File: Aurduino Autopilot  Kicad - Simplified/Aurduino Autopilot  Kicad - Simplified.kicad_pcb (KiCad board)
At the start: 2 copper layers, 79 x 74 mm, 24 parts, among them J1 12V_in, J2 to_clock, J3 to_LCD, J5 to_RTC, SW1 SW_Push, U1 LM350_TO3

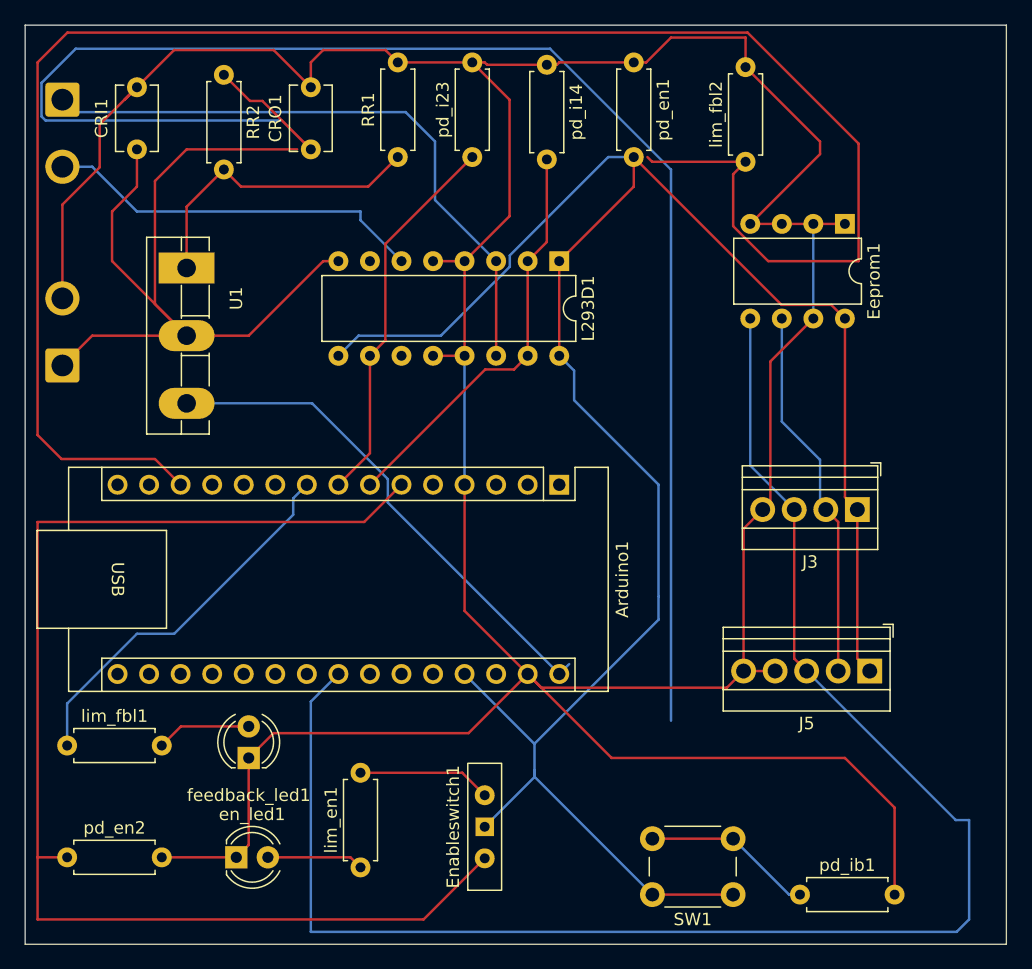
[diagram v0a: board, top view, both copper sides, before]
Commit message: added Simplified kicad design
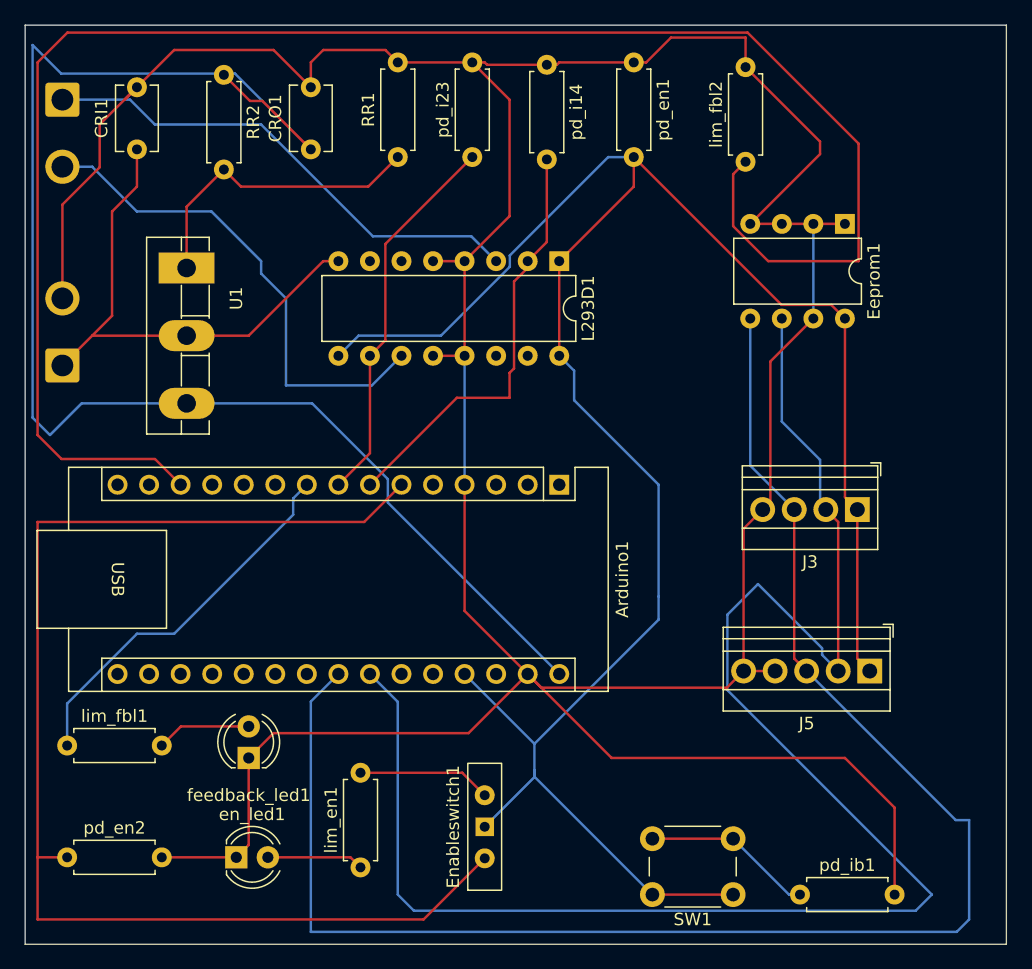
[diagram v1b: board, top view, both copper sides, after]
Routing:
- net Net-(Arduino1-A5): track 30.3 -> 135.5 mm
- net Net-(Arduino1-VIN): track 177.0 -> 119.5 mm
- net +12C: track 70.0 -> 42.2 mm
- net Net-(J2-Pin_2): track 30.9 -> 40.3 mm
- net Net-(J2-Pin_1): track 50.7 -> 41.7 mm
- net Net-(Arduino1-D10): track 148.4 -> 140.3 mm
- net Net-(Arduino1-D4): track 33.4 -> 34.6 mm
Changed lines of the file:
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@@
 	)
 	(segment
-		(start 42 75)
-		(end 36 69)
+		(start 38 60)
+		(end 38 63)
+		(width 0.2)
+		(layer "F.Cu")
+		(net 2)
+	)
+	(segment
+		(start 36 65)
+		(end 36 73.4)
 		(width 0.2)
 		(layer "F.Cu")
@@
 	)
 	(segment
-		(start 38 63)
-		(end 38 60)
-		(width 0.2)
-		(layer "F.Cu")
-		(net 2)
-	)
-	(segment
-		(start 36 65)
-		(end 38 63)
-		(width 0.2)
-		(layer "F.Cu")
-		(net 2)
-	)
-	(segment
-		(start 39.45 62.55)
-		(end 42 60)
-		(width 0.2)
-		(layer "F.Cu")
-		(net 2)
-	)
-	(segment
 		(start 42 75)
 		(end 47 75)
@@
 	)
 	(segment
-		(start 36 69)
-		(end 36 65)
-		(width 0.2)
-		(layer "F.Cu")
-		(net 2)
-	)
-	(segment
-		(start 42 60)
-		(end 50.9 60)
-		(width 0.2)
-		(layer "F.Cu")
-		(net 2)
-	)
-	(segment
-		(start 42 75)
-		(end 39.45 72.45)
+		(start 36 73.4)
+		(end 34.4 75)
 		(width 0.2)
 		(layer "F.Cu")
@@
 	)
 	(segment
-		(start 39.45 72.45)
-		(end 39.45 62.55)
+		(start 38 63)
+		(end 36 65)
 		(width 0.2)
 		(layer "F.Cu")
@@
 	)
 	(segment
-		(start 66.04 77.72)
-		(end 56.76 87)
+		(start 69.46 69.54)
+		(end 68.36 70.64)
 		(width 0.2)
 		(layer "F.Cu")
@@
 	)
 	(segment
-		(start 68.36 77.72)
-		(end 66.04 77.72)
+		(start 56.76 87)
+		(end 63.76 80)
 		(width 0.2)
 		(layer "F.Cu")
@@
 	)
 	(segment
+		(start 63.76 80)
+		(end 68 80)
+		(width 0.2)
+		(layer "F.Cu")
+		(net 3)
+	)
+	(segment
+		(start 68.36 70.64)
+		(end 68.36 77.64)
+		(width 0.2)
+		(layer "F.Cu")
+		(net 3)
+	)
+	(segment
 		(start 69.46 69)
-		(end 69.46 76.62)
-		(width 0.2)
-		(layer "F.Cu")
-		(net 3)
-	)
-	(segment
-		(start 69.46 76.62)
-		(end 68.36 77.72)
+		(end 69.46 69.54)
 		(width 0.2)
 		(layer "F.Cu")
@@
 	)
 	(segment
+		(start 68 80)
+		(end 68 78)
+		(width 0.2)
+		(layer "F.Cu")
+		(net 3)
+	)
+	(segment
+		(start 68.36 77.64)
+		(end 68 78)
+		(width 0.2)
+		(layer "F.Cu")
+		(net 3)
+	)
+	(segment
 		(start 52 53)
 		(end 53 52)
@@
 	)
 	(segment
-		(start 30.640256 57.675)
-		(end 30.325 57.359744)
+		(start 45.9 53.9)
+		(end 31.9 53.9)
 		(width 0.2)
 		(layer "B.Cu")
@@
 	)
 	(segment
+		(start 31 83)
+		(end 33.55 80.45)
+		(width 0.2)
+		(layer "B.Cu")
+		(net 9)
+	)
+	(segment
+		(start 29.6 51.6)
+		(end 29.6 81.6)
+		(width 0.2)
+		(layer "B.Cu")
+		(net 9)
+	)
+	(segment
 		(start 52 60)
-		(end 49.675 57.675)
+		(end 45.9 53.9)
 		(width 0.2)
 		(layer "B.Cu")
@@
 	)
 	(segment
-		(start 42 80.45)
-		(end 41.434365 80.45)
+		(start 33.55 80.45)
+		(end 42 80.45)
 		(width 0.2)
 		(layer "B.Cu")
@@
 	)
 	(segment
-		(start 49.675 57.675)
-		(end 30.640256 57.675)
-		(width 0.2)
-		(layer "B.Cu")
-		(net 9)
-	)
-	(segment
-		(start 81 61.634365)
-		(end 81 106)
-		(width 0.2)
-		(layer "B.Cu")
-		(net 9)
-	)
-	(segment
-		(start 33.065256 51.9)
-		(end 71.265635 51.9)
-		(width 0.2)
-		(layer "B.Cu")
-		(net 9)
-	)
-	(segment
-		(start 72 102.24)
-		(end 72.799999 101.440001)
-		(width 0.2)
-		(layer "B.Cu")
-		(net 9)
-	)
-	(segment
-		(start 30.325 54.640256)
-		(end 33.065256 51.9)
+		(start 31.9 53.9)
+		(end 29.6 51.6)
 		(width 0.2)
 		(layer "B.Cu")
@@
 	)
 	(segment
-		(start 30.325 57.359744)
-		(end 30.325 54.640256)
+		(start 29.6 81.6)
+		(end 31 83)
 		(width 0.2)
 		(layer "B.Cu")
@@
 	)
 	(segment
-		(start 71.265635 51.9)
-		(end 81 61.634365)
-		(width 0.2)
-		(layer "B.Cu")
-		(net 9)
-	)
-	(segment
-		(start 79.48 61)
-		(end 79.1 60.62)
-		(width 0.2)
-		(layer "F.Cu")
-		(net 12)
-	)
-	(segment
 		(start 96.1 59.534315)
 		(end 96.1 69)
@@
 	)
 	(segment
-		(start 87 61)
-		(end 79.48 61)
-		(width 0.2)
-		(layer "F.Cu")
-		(net 12)
-	)
-	(segment
 		(start 30 53)
 		(end 32.4 50.6)
@@
 	)
 	(segment
+		(start 48 69)
+		(end 48 70)
+		(width 0.2)
+		(layer "B.Cu")
+		(net 19)
+	)
+	(segment
 		(start 32 61.4)
 		(end 34.4 61.4)
@@
 	(segment
 		(start 38 65)
-		(end 56 65)
+		(end 44 65)
 		(width 0.2)
 		(layer "B.Cu")
@@
 	)
 	(segment
-		(start 56 65.7)
-		(end 59.3 69)
+		(start 50 79)
+		(end 56.92 79)
+		(width 0.2)
+		(layer "B.Cu")
+		(net 19)
+	)
+	(segment
+		(start 44 65)
+		(end 48 69)
+		(width 0.2)
+		(layer "B.Cu")
+		(net 19)
+	)
+	(segment
+		(start 48 70)
+		(end 50 72)
+		(width 0.2)
+		(layer "B.Cu")
+		(net 19)
+	)
+	(segment
+		(start 56.92 79)
+		(end 59.3 76.62)
 		(width 0.2)
 		(layer "B.Cu")
@@
 	)
 	(segment
-		(start 56 65)
-		(end 56 65.7)
+		(start 50 72)
+		(end 50 79)
 		(width 0.2)
 		(layer "B.Cu")
@@
 	)
 	(segment
-		(start 66.92 69)
-		(end 66.92 76.62)
-		(width 0.2)
-		(layer "F.Cu")
+		(start 64.92 67)
+		(end 66.92 69)
+		(width 0.2)
+		(layer "B.Cu")
 		(net 22)
 	)
 	(segment
-		(start 62 59.36)
-		(end 62 64.08)
+		(start 37.444365 56)
+		(end 32 56)
 		(width 0.2)
 		(layer "B.Cu")
@@
 	)
 	(segment
-		(start 33 57)
-		(end 59.64 57)
+		(start 39.444365 58)
+		(end 37.444365 56)
 		(width 0.2)
 		(layer "B.Cu")
@@
 	)
 	(segment
-		(start 59.64 57)
-		(end 62 59.36)
+		(start 39.444365 58)
+		(end 48 58)
 		(width 0.2)
 		(layer "B.Cu")
@@
 	)
 	(segment
-		(start 62 64.08)
-		(end 66.92 69)
+		(start 57 67)
+		(end 64.92 67)
+		(width 0.2)
+		(layer "B.Cu")
+		(net 22)
+	)
+	(segment
+		(start 48 58)
+		(end 57 67)
 		(width 0.2)
 		(layer "B.Cu")
@@
 	)
 	(segment
+		(start 59 104.48)
+		(end 56.76 102.24)
+		(width 0.2)
+		(layer "B.Cu")
+		(net 39)
+	)
+	(segment
+		(start 93.16 100.16)
+		(end 88 95)
+		(width 0.2)
+		(layer "B.Cu")
+		(net 39)
+	)
+	(segment
+		(start 59 120)
+		(end 59 104.48)
+		(width 0.2)
+		(layer "B.Cu")
+		(net 39)
+	)
+	(segment
 		(start 89.92 81.92)
 		(end 93 85)
@@
 		(width 0.2)
 		(layer "B.Cu")
+		(net 39)
+	)
+	(segment
+		(start 94.46 102)
+		(end 93.16 100.7)
+		(width 0.2)
+		(layer "B.Cu")
+		(net 39)
+	)
+	(segment
+		(start 60.3 121.3)
+		(end 59 120)
+		(width 0.2)
+		(layer "B.Cu")
+		(net 39)
+	)
+	(segment
+		(start 88 95)
+		(end 85.54 97.46)
+		(width 0.2)
+		(layer "B.Cu")
+		(net 39)
+	)
+	(segment
+		(start 100.7 121.3)
+		(end 60.3 121.3)
+		(width 0.2)
+		(layer "B.Cu")
+		(net 39)
+	)
+	(segment
+		(start 102 120)
+		(end 100.7 121.3)
+		(width 0.2)
+		(layer "B.Cu")
+		(net 39)
+	)
+	(segment
+		(start 85.54 97.46)
+		(end 85.54 103.54)
+		(width 0.2)
+		(layer "B.Cu")
+		(net 39)
+	)
+	(segment
+		(start 93.16 100.7)
+		(end 93.16 100.16)
+		(width 0.2)
+		(layer "B.Cu")
+		(net 39)
+	)
+	(segment
+		(start 85.54 103.54)
+		(end 102 120)
+		(width 0.2)
+		(layer "B.Cu")

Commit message: doc
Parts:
- removed lim_fbl2: R, Resistor_THT:R_Axial_DIN0207_L6.3mm_D2.5mm_P7.62mm_Horizontal
- added pd_enable1: R, Resistor_THT:R_Axial_DIN0207_L6.3mm_D2.5mm_P7.62mm_Horizontal, F.Cu at (85.0, 60.6)
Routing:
- net GND: track 304.1 -> 306.1 mm

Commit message: doc
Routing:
- net Net-(Arduino1-A4): track 131.4 -> 129.9 mm
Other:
- board size 79 x 74 mm -> 76 x 74 mm
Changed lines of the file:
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@@
 	(gr_rect
 		(start 29 50)
-		(end 108 124)
+		(end 105 124)
 		(stroke
 			(width 0.05)
@@
 	)
 	(segment
+		(start 103 122)
+		(end 104 123)
+		(width 0.2)
+		(layer "B.Cu")
+		(net 13)
+	)
+	(segment
+		(start 87.38 73.62)
+		(end 87.38 85.46)
+		(width 0.2)
+		(layer "B.Cu")
+		(net 13)
+	)
+	(segment
+		(start 102 112.08)
+		(end 102 117)
+		(width 0.2)
+		(layer "B.Cu")
+		(net 13)
+	)
+	(segment
 		(start 91.92 102)
-		(end 103.92 114)
+		(end 102 112.08)
+		(width 0.2)
+		(layer "B.Cu")
+		(net 13)
+	)
+	(segment
+		(start 52 123)
+		(end 52 104.46)
+		(width 0.2)
+		(layer "B.Cu")
+		(net 13)
+	)
+	(segment
+		(start 104 123)
+		(end 52 123)
 		(width 0.2)
 		(layer "B.Cu")
@@
 	)
 	(segment
-		(start 87.38 73.62)
-		(end 87.38 85.46)
-		(width 0.2)
-		(layer "B.Cu")
-		(net 13)
-	)
-	(segment
-		(start 105 114)
-		(end 105 122)
-		(width 0.2)
-		(layer "B.Cu")
-		(net 13)
-	)
-	(segment
-		(start 52 123)
-		(end 52 104.46)
-		(width 0.2)
-		(layer "B.Cu")
-		(net 13)
-	)
-	(segment
-		(start 103.92 114)
-		(end 105 114)
+		(start 102 117)
+		(end 103 118)
+		(width 0.2)
+		(layer "B.Cu")
+		(net 13)
+	)
+	(segment
+		(start 103 118)
+		(end 103 122)
 		(width 0.2)
 		(layer "B.Cu")
@@
 		(width 0.2)
 		(layer "B.Cu")
-		(net 13)
-	)
-	(segment
-		(start 104 123)
-		(end 52 123)
-		(width 0.2)
-		(layer "B.Cu")
-		(net 13)
-	)
-	(segment
-		(start 105 122)
-		(end 104 123)
-		(width 0.2)
-		(layer "B.Cu")

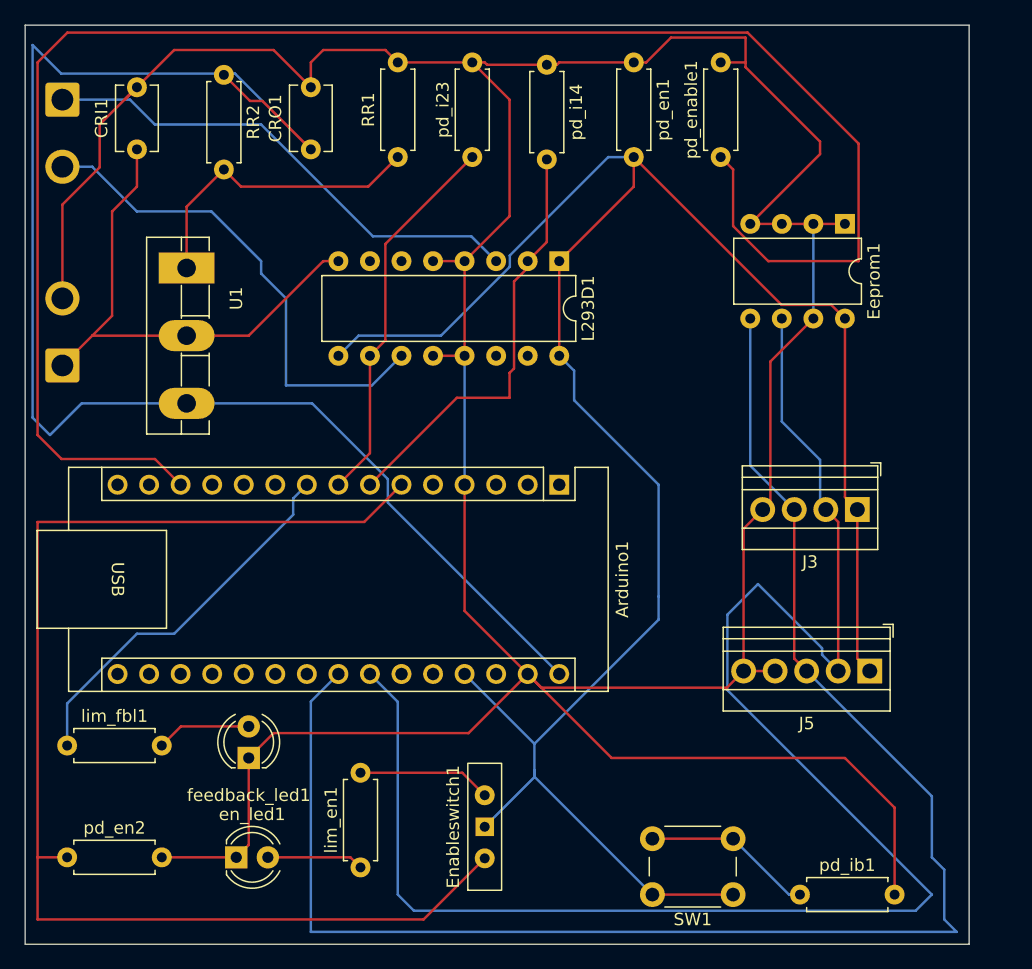
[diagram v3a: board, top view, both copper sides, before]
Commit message: fixed sleep mode, updated diagrams
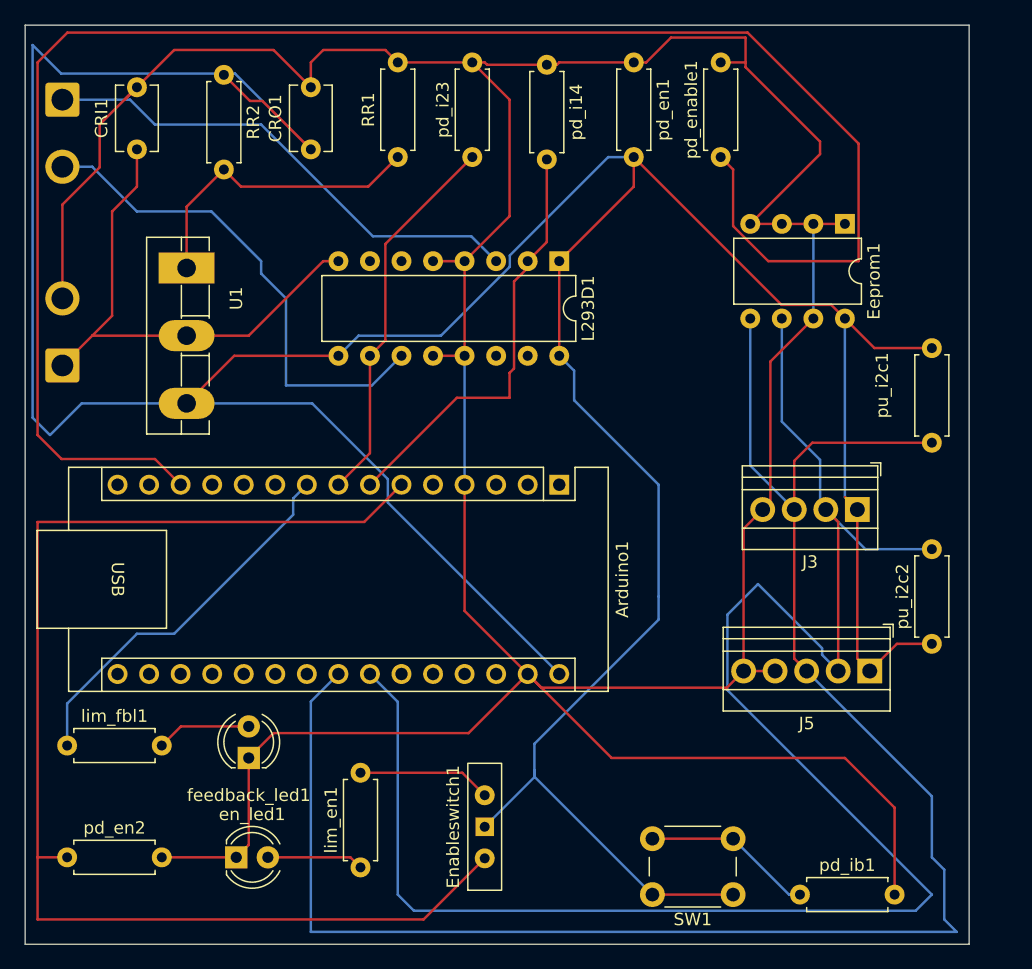
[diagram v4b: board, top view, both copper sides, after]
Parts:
- added pu_i2c1: R, Resistor_THT:R_Axial_DIN0207_L6.3mm_D2.5mm_P7.62mm_Horizontal, F.Cu at (102.0, 76.0)
- added pu_i2c2: R, Resistor_THT:R_Axial_DIN0207_L6.3mm_D2.5mm_P7.62mm_Horizontal, F.Cu at (102.0, 99.8)
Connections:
- Arduino1 pad 27: +5V -> unconnected-(Arduino1-+5V-Pad27)
- Arduino1 pad 30: Net-(Arduino1-VIN) -> +5V
- CRO1 pad 1: Net-(Arduino1-VIN) -> +5V
- RR2 pad 1: Net-(Arduino1-VIN) -> +5V
- U1 pad 3: Net-(Arduino1-VIN) -> +5V
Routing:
- net +5V: track 176.4 -> 317.5 mm
- net Net-(Arduino1-VIN): track 119.5 -> 0.00 mm
- net Net-(Arduino1-A4): track 129.9 -> 145.5 mm
- net Net-(Arduino1-A5): track 135.5 -> 145.4 mm
